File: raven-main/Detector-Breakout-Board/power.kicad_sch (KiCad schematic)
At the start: 24 parts, among them J1 XT60PW-M, Q1 SQJQ100EL, T1 Transformer_1P_1S, U6 LM5185QPWPRQ1, U7 TPS7A4701xRGW

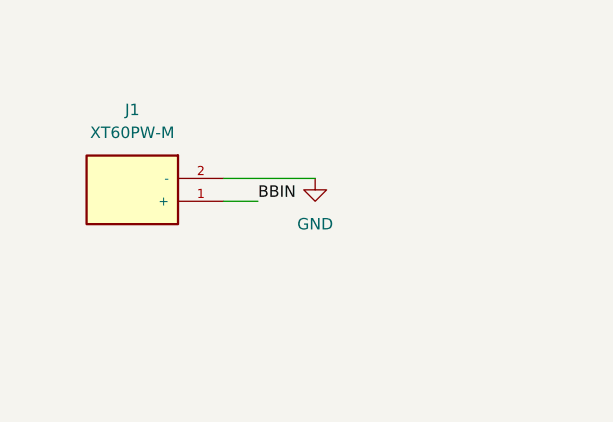
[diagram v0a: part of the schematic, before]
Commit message: Added power and output pins
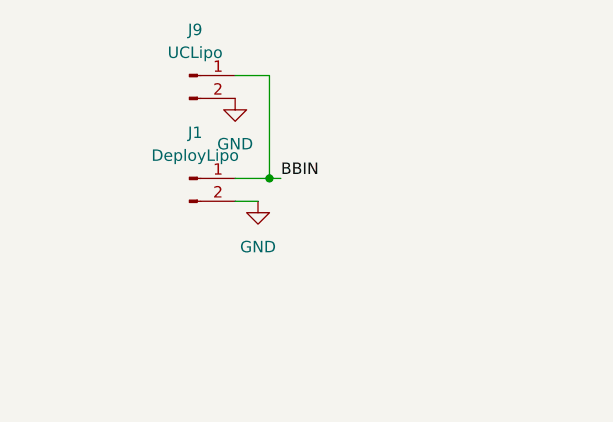
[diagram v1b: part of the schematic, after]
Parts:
- removed J1: XT60PW-M, AMASS_XT60PW-M, symbol iclr:XT60PW-M
- added J1: DeployLipo, TerminalBlock_Phoenix:TerminalBlock_Phoenix_MKDS-3-2-5.08_1x02_P5.08mm_Horizontal, symbol Connector:Conn_01x02_Male
- added J9: UCLipo, Connector_JST:JST_PH_B2B-PH-K_1x02_P2.00mm_Vertical, symbol Connector:Conn_01x02_Male
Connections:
- net +50V: now also J1.1 (Pin_1), J1.2 (Pin_2), J9.1 (Pin_1), J9.2 (Pin_2)

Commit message: Changed detector output to 3.3V
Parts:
- added C45: 10uF, Capacitor_SMD:C_0402_1005Metric, symbol Device:C_Small
- added C46: 1uF, Capacitor_SMD:C_0402_1005Metric, symbol Device:C_Small
- added C47: 47uF, Capacitor_SMD:C_0402_1005Metric, symbol Device:C_Small
- added R38: 13.3k, Resistor_SMD:R_0402_1005Metric, symbol Device:R_Small
- added R39: 9.76k, Resistor_SMD:R_0402_1005Metric, symbol Device:R_Small
- added U8: TPS7A4701xRGW, Package_DFN_QFN:Texas_RGW0020A_VQFN-20-1EP_5x5mm_P0.65mm_EP3.15x3.15mm_ThermalVias, symbol Regulator_Linear:TPS7A4701xRGW
- R22: value 10k -> 9.76k
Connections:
- net +50V: now also C45.1, C45.2, C46.2, C47.2, R39.2, U8.13 (EN), U8.15 (IN), U8.16 (IN), U8.7 (GND)
- new net: C46.1, U8.14 (NR)
- new net: R38.2, R39.1, U8.3 (SENSE/FB)
- new net +3V3: C47.1, R38.1, U8.1 (OUT), U8.20 (OUT)
- no-connect marks 12 -> 20
